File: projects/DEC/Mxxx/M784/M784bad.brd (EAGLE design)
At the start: 125.7 x 62.2 mm, 11 parts

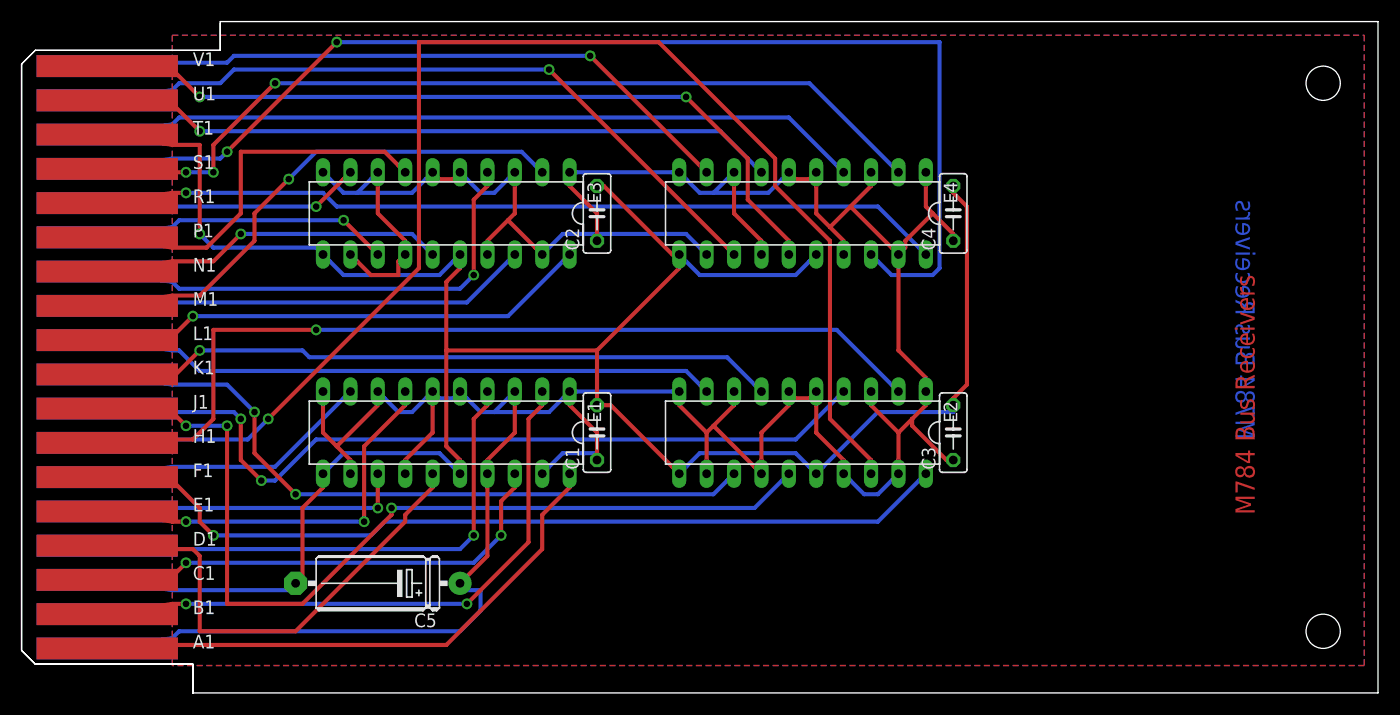
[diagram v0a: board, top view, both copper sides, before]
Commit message: Fix references to the 75als057 to actually find the part in dec-con.
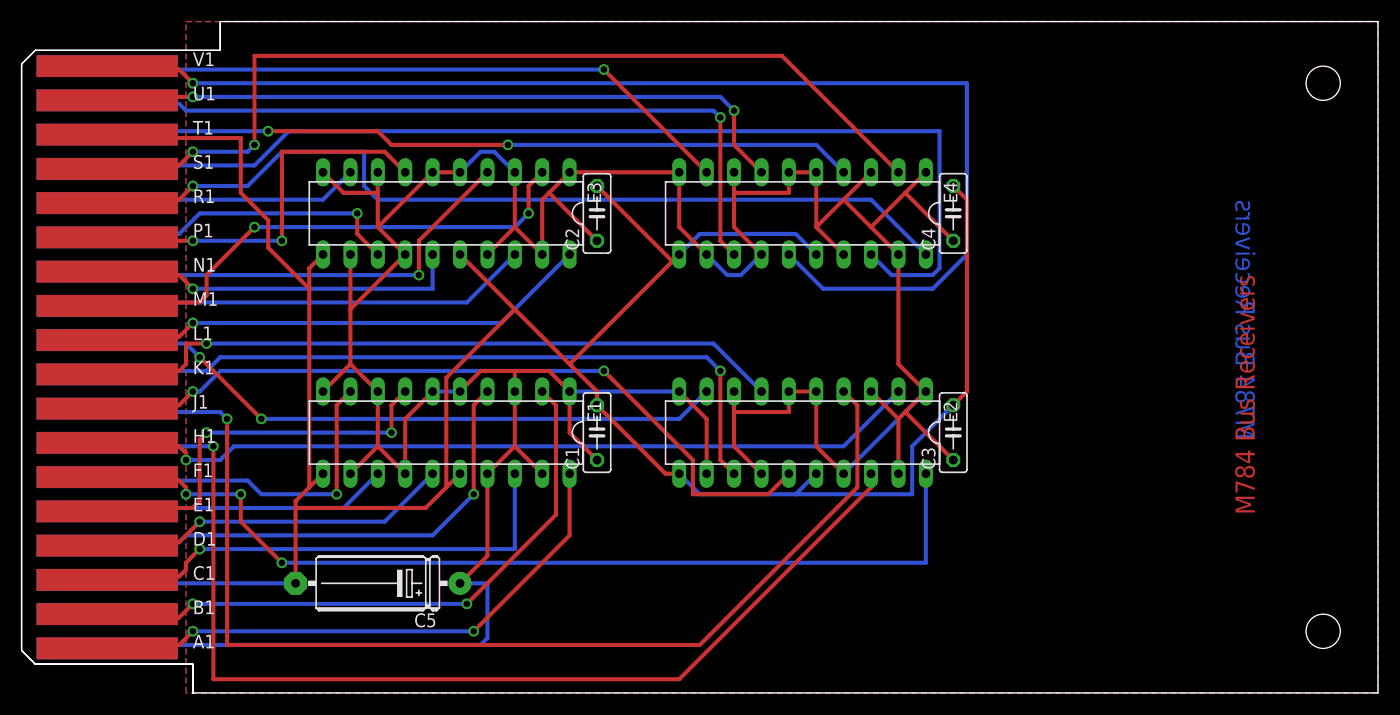
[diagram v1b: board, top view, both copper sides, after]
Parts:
- E1, E2, E3, E4: value 75ALS057 -> SN75ALS057
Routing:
- net N$12: track 73.3 -> 115.4 mm, vias 2 -> 1
- net N$21: track 76.6 -> 106.3 mm, vias 2 -> 1
- net N$22: track 126.8 -> 101.2 mm
- net GND: track 225.3 -> 240.0 mm, vias 1 -> 0
- net N$20: track 85.6 -> 72.0 mm, vias 3 -> 2
- net N$28: track 44.6 -> 32.9 mm, vias 0 -> 1
- net N$14: track 110.1 -> 98.7 mm, vias 2 -> 0
- net N$24: track 81.1 -> 89.3 mm, vias 1 -> 3
- net N$23: track 84.8 -> 77.0 mm
- net N$25: track 25.5 -> 32.0 mm, vias 0 -> 1
- net N$15: track 78.3 -> 83.7 mm
- net N$16: track 81.7 -> 87.0 mm, vias 3 -> 2
- net N$10: track 66.1 -> 70.7 mm
- net N$4: track 44.9 -> 41.2 mm
- net N$17: track 65.4 -> 68.1 mm, vias 2 -> 1
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
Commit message: Walk the project tree, making things pass current design rules.
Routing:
- net N$12: track 115.4 -> 77.0 mm, vias 1 -> 0
- net N$21: track 106.3 -> 70.0 mm, vias 1 -> 0
- net N$10: track 70.7 -> 106.6 mm, vias 1 -> 0
- net N$14: track 98.7 -> 74.1 mm
- net N$23: track 77.0 -> 100.3 mm, vias 1 -> 0
- net VCC: track 362.9 -> 344.5 mm
- net N$18: track 59.6 -> 74.3 mm, vias 2 -> 0
- net N$15: track 83.7 -> 96.3 mm, vias 1 -> 0
- net N$22: track 101.2 -> 91.6 mm
- net GND: track 240.0 -> 230.7 mm, vias 0 -> 1
- net N$16: track 87.0 -> 77.7 mm, vias 2 -> 1
- net N$24: track 89.3 -> 98.1 mm, vias 3 -> 2
- net N$32: track 52.9 -> 60.7 mm, vias 2 -> 1
- net N$6: track 36.8 -> 30.5 mm
- net N$25: track 32.0 -> 26.6 mm
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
